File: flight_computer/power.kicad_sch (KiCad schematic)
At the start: 28 parts, among them J3 Conn_01x02, Q2 Q_NMOS_GSD, U2 Opamp_Quad, U3 TPS63051RMWR, U4 MIC94310-GYMT-TR

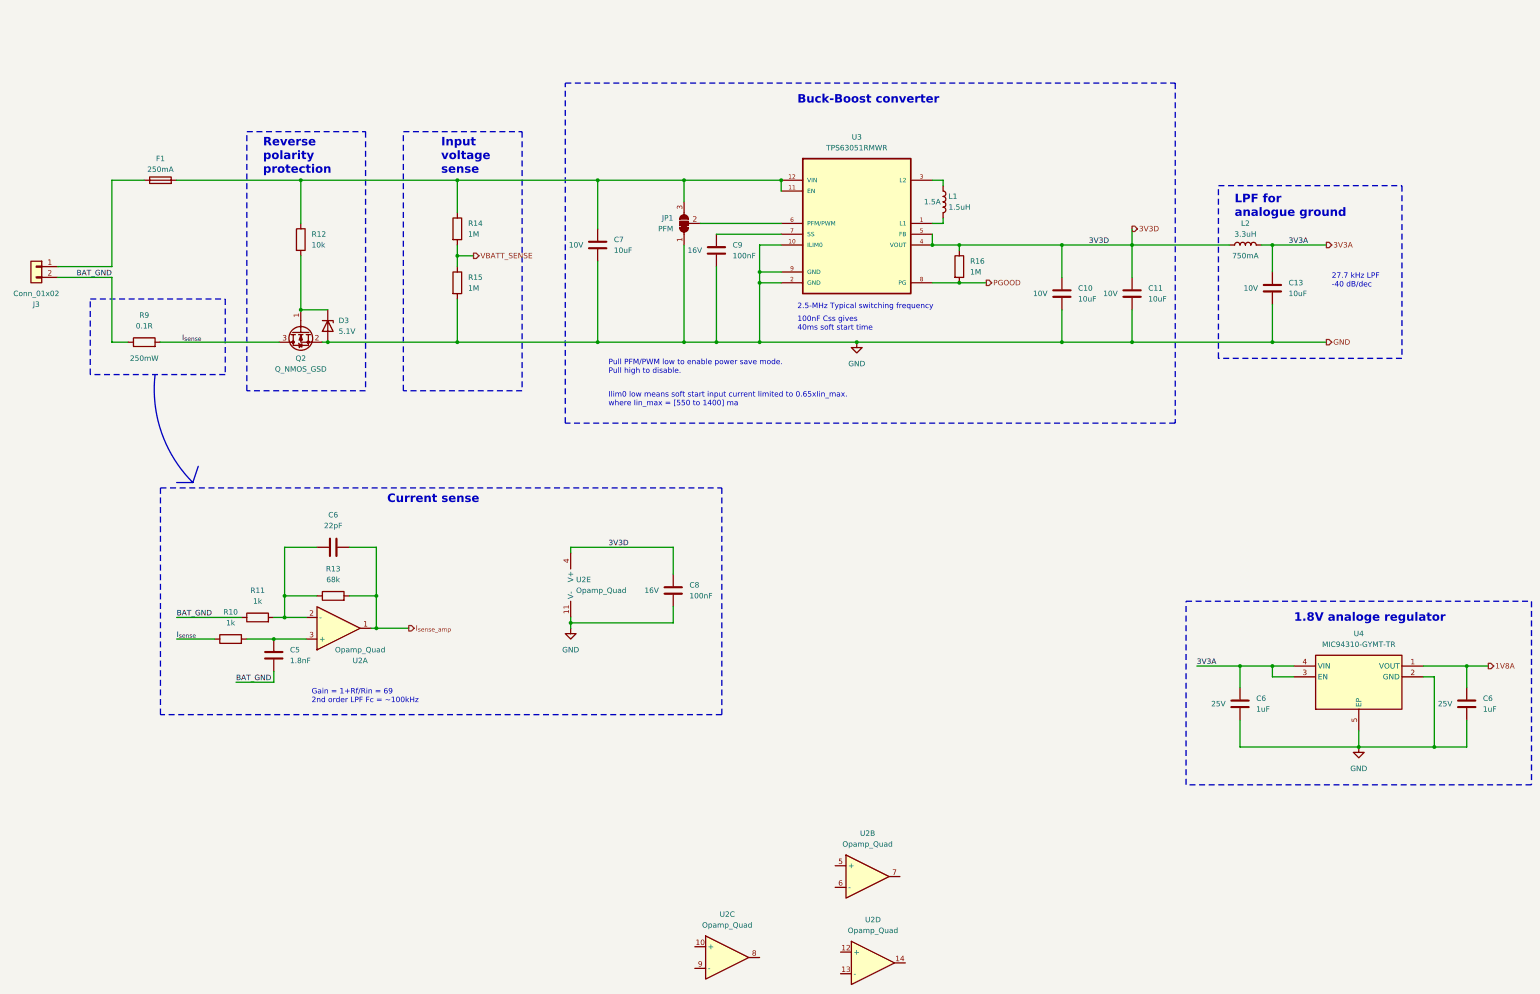
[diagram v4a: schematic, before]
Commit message: Finishing gps, ready to connect all
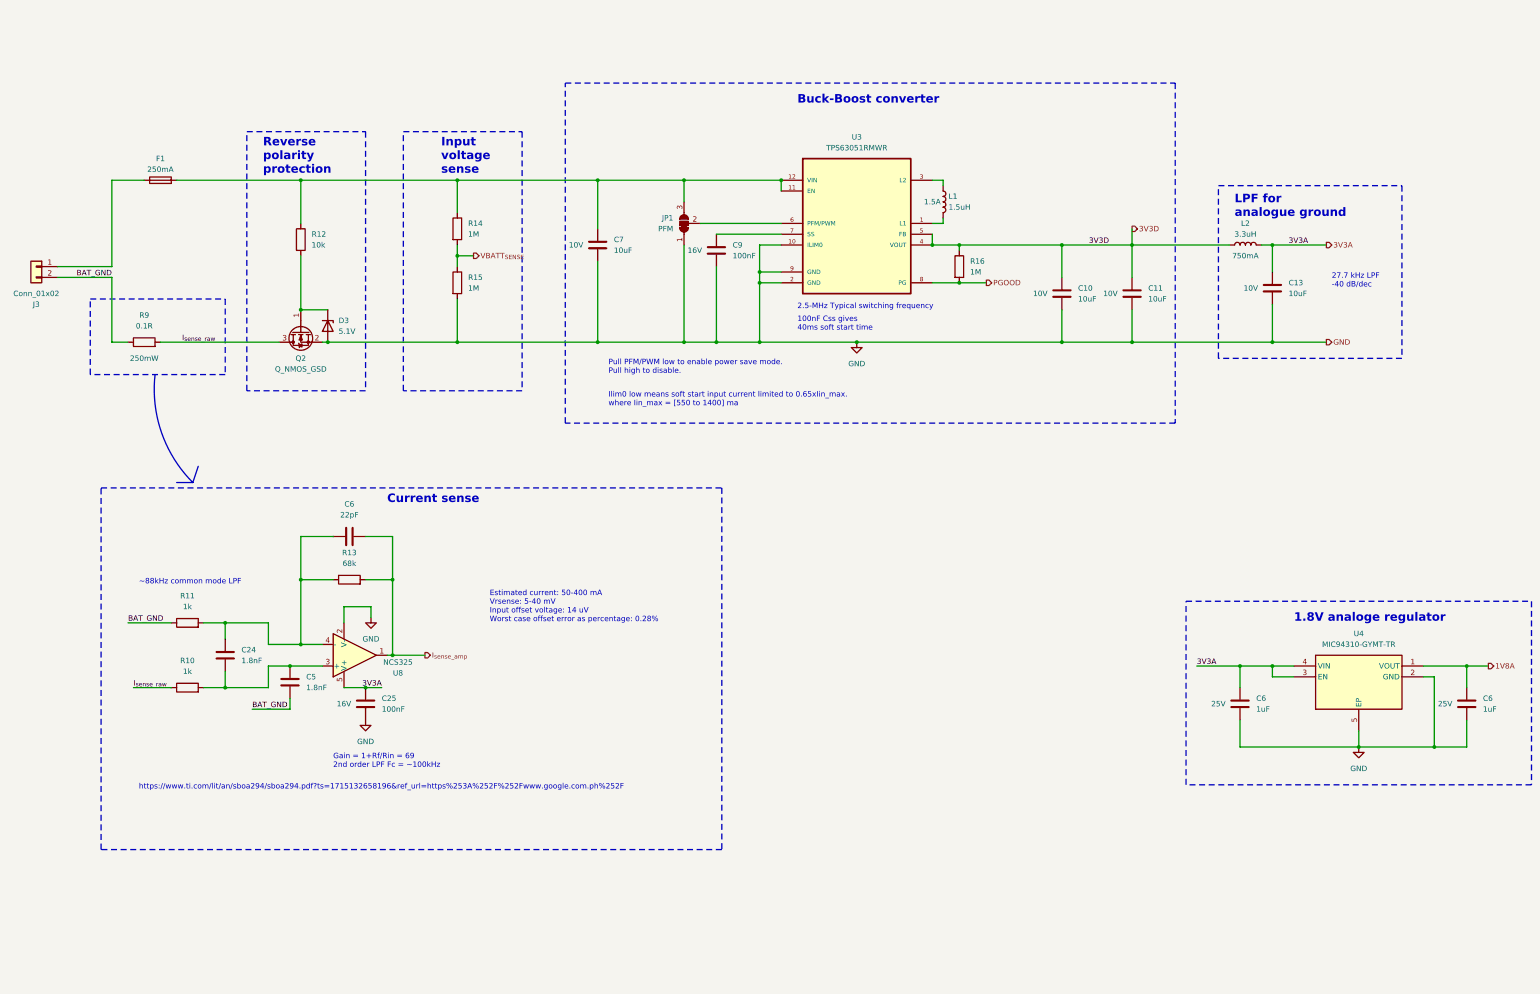
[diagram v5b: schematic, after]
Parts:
- removed C8: 100nF, Capacitor_SMD:C_0402_1005Metric, symbol Device:C
- removed U2: Opamp_Quad, Package_SO:SOIC-14_3.9x8.7mm_P1.27mm, symbol Device:Opamp_Quad
- added C24: 1.8nF, Capacitor_SMD:C_0402_1005Metric, symbol Device:C
- added C25: 100nF, Capacitor_SMD:C_0402_1005Metric, symbol Device:C
- added U8: NCS325, Package_TO_SOT_SMD:SOT-23-5, symbol Amplifier_Operational:NCS325
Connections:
- net 3V3A: now also C25.1, U8.5 (V+)
- net GND: now also C25.2, U8.2 (V-)
- net I_{sense_amp}: now also U8.1
- net at C5.1, R10.2: now also C24.2, U8.3 (+)
- net at C6.2, R11.2, R13.1: now also C24.1, U8.4 (-)
- net I_{sense} renamed I_{sense_raw}
- net VBATT_SENSE renamed VBATT_{SENSE}
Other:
- note added: "Estimated current: 50-400 mA Vrsense: 5-40 mV Input offset voltage: 14 uV Worst case offset error as percentage: 0.28%"
- note added: "https://www.ti.com/lit/an/sboa294/sboa294.pdf?ts=1715132658196&ref_url=https%253A%252F%252Fwww.google.com.ph%252F"
- note added: "~88kHz common mode LPF"
- moved on the sheet: C5, C6, R10, R11, R13

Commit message: ERC complete
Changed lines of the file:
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@@
   (junction (at 85.09 67.31) (diameter 0) (color 0 0 0 0)
   )
+  (junction (at 355.6 181.61) (diameter 0) (color 0 0 0 0)
+  )
   (junction (at 154.94 67.31) (diameter 0) (color 0 0 0 0)
   )
@@
   (junction (at 198.12 67.31) (diameter 0) (color 0 0 0 0)
   )
+  (junction (at 256.54 82.55) (diameter 0) (color 0 0 0 0)
+  )
   (junction (at 182.88 105.41) (diameter 0) (color 0 0 0 0)
   )
@@
   (junction (at 193.04 91.44) (diameter 0) (color 0 0 0 0)
   )
+  (junction (at 228.6 105.41) (diameter 0) (color 0 0 0 0)
+  )
   (junction (at 240.03 82.55) (diameter 0) (color 0 0 0 0)
   )
@@
   (junction (at 175.26 67.31) (diameter 0) (color 0 0 0 0)
   )
+  (junction (at 328.93 82.55) (diameter 0) (color 0 0 0 0)
+  )
   (junction (at 121.92 67.31) (diameter 0) (color 0 0 0 0)
   )
+  (junction (at 40.64 93.98) (diameter 0) (color 0 0 0 0)
+  )
   (junction (at 154.94 105.41) (diameter 0) (color 0 0 0 0)
   )
+  (junction (at 40.64 74.93) (diameter 0) (color 0 0 0 0)
+  )
   (junction (at 215.9 105.41) (diameter 0) (color 0 0 0 0)
   )
@@
     (stroke (width 0) (type default))
   )
-  (wire (pts (xy 215.9 105.41) (xy 264.16 105.41))
+  (wire (pts (xy 215.9 105.41) (xy 228.6 105.41))
     (stroke (width 0) (type default))
   )
@@
     (stroke (width 0) (type default))
   )
-  (wire (pts (xy 40.64 90.17) (xy 40.64 105.41))
+  (wire (pts (xy 40.64 90.17) (xy 40.64 93.98))
+    (stroke (width 0) (type default))
+  )
+  (wire (pts (xy 328.93 82.55) (xy 335.28 82.55))
     (stroke (width 0) (type default))
   )
@@
     (stroke (width 0) (type default))
   )
+  (wire (pts (xy 256.54 82.55) (xy 264.16 82.55))
+    (stroke (width 0) (type default))
+  )
   (wire (pts (xy 313.69 181.61) (xy 318.77 181.61))
     (stroke (width 0) (type default))
@@
     (stroke (width 0) (type default))
   )
-  (wire (pts (xy 313.69 82.55) (xy 326.39 82.55))
-    (stroke (width 0) (type default))
-  )
   (wire (pts (xy 179.07 77.47) (xy 198.12 77.47))
     (stroke (width 0) (type default))
@@
     (stroke (width 0) (type default))
   )
-  (wire (pts (xy 40.64 67.31) (xy 40.64 87.63))
+  (wire (pts (xy 40.64 67.31) (xy 40.64 74.93))
     (stroke (width 0) (type default))
   )
@@
     (stroke (width 0) (type default))
   )
+  (wire (pts (xy 355.6 181.61) (xy 349.25 181.61))
+    (stroke (width 0) (type default))
+  )
   (wire (pts (xy 121.92 67.31) (xy 154.94 67.31))
     (stroke (width 0) (type default))
@@
     (stroke (width 0) (type default))
   )
+  (wire (pts (xy 40.64 74.93) (xy 40.64 87.63))
+    (stroke (width 0) (type default))
+  )
   (wire (pts (xy 91.44 97.79) (xy 85.09 97.79))
     (stroke (width 0) (type default))
@@
     (stroke (width 0) (type default))
   )
+  (wire (pts (xy 40.64 93.98) (xy 40.64 105.41))
+    (stroke (width 0) (type default))
+  )
   (wire (pts (xy 215.9 105.41) (xy 193.04 105.41))
     (stroke (width 0) (type default))
   )
+  (wire (pts (xy 228.6 105.41) (xy 264.16 105.41))
+    (stroke (width 0) (type default))
+  )
   (wire (pts (xy 101.6 167.64) (xy 101.6 170.18))
     (stroke (width 0) (type default))
@@
     (stroke (width 0) (type default))
   )
-  (wire (pts (xy 240.03 82.55) (xy 264.16 82.55))
+  (wire (pts (xy 240.03 82.55) (xy 256.54 82.55))
     (stroke (width 0) (type default))
   )
@@
     (stroke (width 0) (type default))
   )
+  (wire (pts (xy 313.69 82.55) (xy 328.93 82.55))
+    (stroke (width 0) (type default))
+  )
   (wire (pts (xy 44.45 171.45) (xy 54.61 171.45))
     (stroke (width 0) (type default))
@@
     (stroke (width 0) (type default))
   )
-  (wire (pts (xy 359.41 181.61) (xy 349.25 181.61))
+  (wire (pts (xy 359.41 181.61) (xy 355.6 181.61))
     (stroke (width 0) (type default))
   )
@@
     (effects (font (size 1.27 1.27)) (justify left))
   )
-  (hierarchical_label "3V3A" (shape output) (at 326.39 82.55 0) (fields_autoplaced)
+  (hierarchical_label "3V3A" (shape output) (at 335.28 82.55 0) (fields_autoplaced)
     (effects (font (size 1.27 1.27)) (justify left))
   )
@@
     )
   )
+  (symbol (lib_id "power:PWR_FLAG") (at 40.64 93.98 270) (unit 1)
+    (in_bom yes) (on_board yes) (dnp no) (fields_autoplaced)
+    (property "Reference" "#FLG02" (at 42.545 93.98 0)
+      (effects (font (size 1.27 1.27)) hide)
+    )
+    (property "Value" "PWR_FLAG" (at 44.45 93.98 90)
+      (effects (font (size 1.27 1.27)) (justify left))
+    )
+    (property "Footprint" "" (at 40.64 93.98 0)
+      (effects (font (size 1.27 1.27)) hide)
+    )
+    (property "Datasheet" "~" (at 40.64 93.98 0)
+      (effects (font (size 1.27 1.27)) hide)
+    )
+    (pin "1")
+    (instances
+      (project "flight_computer"
+        (path "/89a81c02-14e9-456f-a334-ff69a24bd093/ebc948db-a9d3-410a-bdbf-1c31db890e56"
+          (reference "#FLG02") (unit 1)
+        )
+      )
+    )
+  )
   (symbol (lib_id "Device:R") (at 96.52 161.29 90) (unit 1)
     (in_bom yes) (on_board yes) (dnp no) (fields_autoplaced)
@@
         (path "/89a81c02-14e9-456f-a334-ff69a24bd093/ebc948db-a9d3-410a-bdbf-1c31db890e56"
           (reference "F1") (unit 1)
+        )
+      )
+    )
+  )
+  (symbol (lib_id "power:PWR_FLAG") (at 256.54 82.55 0) (unit 1)
+    (in_bom yes) (on_board yes) (dnp no) (fields_autoplaced)
+    (property "Reference" "#FLG03" (at 256.54 80.645 0)
+      (effects (font (size 1.27 1.27)) hide)
+    )
+    (property "Value" "PWR_FLAG" (at 256.54 77.47 0)
+      (effects (font (size 1.27 1.27)))
+    )
+    (property "Footprint" "" (at 256.54 82.55 0)
+      (effects (font (size 1.27 1.27)) hide)
+    )
+    (property "Datasheet" "~" (at 256.54 82.55 0)
+      (effects (font (size 1.27 1.27)) hide)
+    )
+    (pin "1")
+    (instances
+      (project "flight_computer"
+        (path "/89a81c02-14e9-456f-a334-ff69a24bd093/ebc948db-a9d3-410a-bdbf-1c31db890e56"
+          (reference "#FLG03") (unit 1)
         )
       )
@@
     )
   )
+  (symbol (lib_id "power:PWR_FLAG") (at 328.93 82.55 0) (unit 1)
+    (in_bom yes) (on_board yes) (dnp no) (fields_autoplaced)
+    (property "Reference" "#FLG04" (at 328.93 80.645 0)
+      (effects (font (size 1.27 1.27)) hide)
+    )
+    (property "Value" "PWR_FLAG" (at 328.93 77.47 0)
+      (effects (font (size 1.27 1.27)))
+    )
+    (property "Footprint" "" (at 328.93 82.55 0)
+      (effects (font (size 1.27 1.27)) hide)
+    )
+    (property "Datasheet" "~" (at 328.93 82.55 0)
+      (effects (font (size 1.27 1.27)) hide)
+    )
+    (pin "1")
+    (instances
+      (project "flight_computer"
+        (path "/89a81c02-14e9-456f-a334-ff69a24bd093/ebc948db-a9d3-410a-bdbf-1c31db890e56"
+          (reference "#FLG04") (unit 1)
+        )
+      )
+    )
+  )
   (symbol (lib_id "power:GND") (at 100.33 194.31 0) (unit 1)
     (in_bom yes) (on_board yes) (dnp no) (fields_autoplaced)
@@
         (path "/89a81c02-14e9-456f-a334-ff69a24bd093/ebc948db-a9d3-410a-bdbf-1c31db890e56"
           (reference "U8") (unit 1)
+        )
+      )
+    )
+  )
+  (symbol (lib_id "power:PWR_FLAG") (at 228.6 105.41 180) (unit 1)
+    (in_bom yes) (on_board yes) (dnp no) (fields_autoplaced)
+    (property "Reference" "#FLG06" (at 228.6 107.315 0)
+      (effects (font (size 1.27 1.27)) hide)
+    )
+    (property "Value" "PWR_FLAG" (at 228.6 110.49 0)
+      (effects (font (size 1.27 1.27)))
+    )
+    (property "Footprint" "" (at 228.6 105.41 0)
+      (effects (font (size 1.27 1.27)) hide)
+    )
+    (property "Datasheet" "~" (at 228.6 105.41 0)
+      (effects (font (size 1.27 1.27)) hide)
+    )
+    (pin "1")
+    (instances
+      (project "flight_computer"
+        (path "/89a81c02-14e9-456f-a334-ff69a24bd093/ebc948db-a9d3-410a-bdbf-1c31db890e56"
+          (reference "#FLG06") (unit 1)
         )
       )
@@
     )
   )
+  (symbol (lib_id "power:PWR_FLAG") (at 40.64 74.93 90) (unit 1)
+    (in_bom yes) (on_board yes) (dnp no) (fields_autoplaced)
+    (property "Reference" "#FLG01" (at 38.735 74.93 0)
+      (effects (font (size 1.27 1.27)) hide)
+    )
+    (property "Value" "PWR_FLAG" (at 36.83 74.93 90)
+      (effects (font (size 1.27 1.27)) (justify left))
+    )
+    (property "Footprint" "" (at 40.64 74.93 0)
+      (effects (font (size 1.27 1.27)) hide)
+    )
+    (property "Datasheet" "~" (at 40.64 74.93 0)
+      (effects (font (size 1.27 1.27)) hide)
+    )
+    (pin "1")
+    (instances
+      (project "flight_computer"
+        (path "/89a81c02-14e9-456f-a334-ff69a24bd093/ebc948db-a9d3-410a-bdbf-1c31db890e56"
+          (reference "#FLG01") (unit 1)
+        )
+      )
+    )
+  )
   (symbol (lib_id "Device:R") (at 121.92 78.74 0) (unit 1)
     (in_bom yes) (on_board yes) (dnp no) (fields_autoplaced)
@@
         )
       )
+    )
+  )
+  (symbol (lib_id "power:PWR_FLAG") (at 355.6 181.61 0) (unit 1)
+    (in_bom yes) (on_board yes) (dnp no) (fields_autoplaced)
+    (property "Reference" "#FLG05" (at 355.6 179.705 0)
+      (effects (font (size 1.27 1.27)) hide)
+    )
+    (property "Value" "PWR_FLAG" (at 355.6 176.53 0)
+      (effects (font (size 1.27 1.27)))
+    )
+    (property "Footprint" "" (at 355.6 181.61 0)
+      (effects (font (size 1.27 1.27)) hide)
+    )
+    (property "Datasheet" "~" (at 355.6 181.61 0)
+      (effects (font (size 1.27 1.27)) hide)
+    )
+    (pin "1")
+    (instances
+      (project "flight_computer"
+        (path "/89a81c02-14e9-456f-a334-ff69a24bd093/ebc948db-a9d3-410a-bdbf-1c31db890e56"
+          (reference "#FLG05") (unit 1)
+        )
+      )

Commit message: Part way through review
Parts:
- renumbered C9 to C10, C10 to C11, C11 to C12, C13 to C14, C24 to C5, C5 to C6, C6 to C7, C25 to C8, C7 to C9, R11 to R10, R10 to R11, U8 to U2

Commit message: Adding shauns thermcoouple
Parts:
- renumbered C5 to C13, C6 to C14, C7 to C15, C8 to C16, C9 to C17, C10 to C18, C11 to C19, C12 to C20, C14 to C22
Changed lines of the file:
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@@
   (symbol (lib_id "Device:C") (at 82.55 185.42 0) (unit 1)
     (in_bom yes) (on_board yes) (dnp no) (fields_autoplaced)
-    (property "Reference" "C6" (at 86.36 184.15 0)
+    (property "Reference" "C14" (at 86.36 184.15 0)
       (effects (font (size 1.27 1.27)) (justify left))
     )
@@
       (project "flight_computer"
         (path "/89a81c02-14e9-456f-a334-ff69a24bd093/ebc948db-a9d3-410a-bdbf-1c31db890e56"
-          (reference "C6") (unit 1)
+          (reference "C14") (unit 1)
         )
       )
@@
   (symbol (lib_id "Device:C") (at 100.33 190.5 0) (unit 1)
     (in_bom yes) (on_board yes) (dnp no)
-    (property "Reference" "C8" (at 104.14 189.23 0)
+    (property "Reference" "C16" (at 104.14 189.23 0)
       (effects (font (size 1.27 1.27)) (justify left))
     )
@@
       (project "flight_computer"
         (path "/89a81c02-14e9-456f-a334-ff69a24bd093/ebc948db-a9d3-410a-bdbf-1c31db890e56"
-          (reference "C8") (unit 1)
+          (reference "C16") (unit 1)
         )
       )
@@
   (symbol (lib_id "Device:C") (at 96.52 151.13 270) (unit 1)
     (in_bom yes) (on_board yes) (dnp no)
-    (property "Reference" "C7" (at 96.52 143.51 90)
+    (property "Reference" "C15" (at 96.52 143.51 90)
       (effects (font (size 1.27 1.27)))
     )
@@
       (project "flight_computer"
         (path "/89a81c02-14e9-456f-a334-ff69a24bd093/ebc948db-a9d3-410a-bdbf-1c31db890e56"
-          (reference "C7") (unit 1)
+          (reference "C15") (unit 1)
         )
       )
@@
   (symbol (lib_id "Device:C") (at 67.31 179.07 0) (unit 1)
     (in_bom yes) (on_board yes) (dnp no) (fields_autoplaced)
-    (property "Reference" "C5" (at 71.12 177.8 0)
+    (property "Reference" "C13" (at 71.12 177.8 0)
       (effects (font (size 1.27 1.27)) (justify left))
     )
@@
       (project "flight_computer"
         (path "/89a81c02-14e9-456f-a334-ff69a24bd093/ebc948db-a9d3-410a-bdbf-1c31db890e56"
-          (reference "C5") (unit 1)
+          (reference "C13") (unit 1)
         )
       )
@@
   (symbol (lib_id "Device:C") (at 182.88 83.82 0) (unit 1)
     (in_bom yes) (on_board yes) (dnp no)
-    (property "Reference" "C10" (at 186.69 82.55 0)
+    (property "Reference" "C18" (at 186.69 82.55 0)
       (effects (font (size 1.27 1.27)) (justify left))
     )
@@
       (project "flight_computer"
         (path "/89a81c02-14e9-456f-a334-ff69a24bd093/ebc948db-a9d3-410a-bdbf-1c31db890e56"
-          (reference "C10") (unit 1)
+          (reference "C18") (unit 1)
         )
       )
@@
         )
         (path "/89a81c02-14e9-456f-a334-ff69a24bd093/ebc948db-a9d3-410a-bdbf-1c31db890e56"
-          (reference "C13") (unit 1)
+          (reference "C21") (unit 1)
         )
       )
@@
   (symbol (lib_id "Device:C") (at 264.16 93.98 0) (unit 1)
     (in_bom yes) (on_board yes) (dnp no)
-    (property "Reference" "C11" (at 267.97 92.71 0)
+    (property "Reference" "C19" (at 267.97 92.71 0)
       (effects (font (size 1.27 1.27)) (justify left))
     )
@@
       (project "flight_computer"
         (path "/89a81c02-14e9-456f-a334-ff69a24bd093/ebc948db-a9d3-410a-bdbf-1c31db890e56"
-          (reference "C11") (unit 1)
+          (reference "C19") (unit 1)
         )
       )
@@
   (symbol (lib_id "Device:C") (at 280.67 93.98 0) (unit 1)
     (in_bom yes) (on_board yes) (dnp no)
-    (property "Reference" "C12" (at 284.48 92.71 0)
+    (property "Reference" "C20" (at 284.48 92.71 0)
       (effects (font (size 1.27 1.27)) (justify left))
     )
@@
       (project "flight_computer"
         (path "/89a81c02-14e9-456f-a334-ff69a24bd093/ebc948db-a9d3-410a-bdbf-1c31db890e56"
-          (reference "C12") (unit 1)
+          (reference "C20") (unit 1)
         )
       )
@@
   (symbol (lib_id "Device:C") (at 313.69 92.71 0) (unit 1)
     (in_bom yes) (on_board yes) (dnp no)
-    (property "Reference" "C14" (at 317.5 91.44 0)
+    (property "Reference" "C22" (at 317.5 91.44 0)
       (effects (font (size 1.27 1.27)) (justify left))
     )
@@
       (project "flight_computer"
         (path "/89a81c02-14e9-456f-a334-ff69a24bd093/ebc948db-a9d3-410a-bdbf-1c31db890e56"
-          (reference "C14") (unit 1)
+          (reference "C22") (unit 1)
         )
       )
@@
   (symbol (lib_id "Device:C") (at 154.94 82.55 0) (unit 1)
     (in_bom yes) (on_board yes) (dnp no)
-    (property "Reference" "C9" (at 158.75 81.28 0)
+    (property "Reference" "C17" (at 158.75 81.28 0)
       (effects (font (size 1.27 1.27)) (justify left))
     )
@@
       (project "flight_computer"
         (path "/89a81c02-14e9-456f-a334-ff69a24bd093/ebc948db-a9d3-410a-bdbf-1c31db890e56"
-          (reference "C9") (unit 1)
+          (reference "C17") (unit 1)
         )
       )
@@
         )
         (path "/89a81c02-14e9-456f-a334-ff69a24bd093/ebc948db-a9d3-410a-bdbf-1c31db890e56"
-          (reference "C15") (unit 1)
-        )
-      )
+          (reference "C23") (unit 1)
+        )
+      )
